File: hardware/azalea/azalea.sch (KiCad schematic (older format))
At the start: 71 parts, among them J1 USB-MICRO-B-SHIELDED, J2 USB-MICRO-B-SHIELDED, U1 LPC43XXFBD144, X1 XTAL4PIN

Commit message: azalea: neighbor interface
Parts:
- added FB? (x2): FILTER, symbol FILTER
- added P?: SPIFI_CS, symbol CONN_01X01
- added P?: LED1, symbol CONN_01X01
- added P?: LED2, symbol CONN_01X01
- added P?: LED3, symbol CONN_01X01
- added P?: LED4, symbol CONN_01X01
- added P?: USB1_VBUS, symbol CONN_01X01
- added P?: USB1_SENSE, symbol CONN_01X01
- added P?: USB1_EN, symbol CONN_01X01
- added P?: USB1_FAULT, symbol CONN_01X01
- added P?: USB1_ID, symbol CONN_01X01
- added P?: USB0_ID, symbol CONN_01X01
- added P?: P2_9, symbol CONN_01X01
- U1: value LPC43XXFBD144 -> LPC4330FBD144
- gave numbers to parts that had none: 2
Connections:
- net !CTS is gone; now on net P1_11: U1.55 (P1_11)
- net !DCD is gone; now on net P1_12: U1.56 (P1_12)
- net !DSR is gone; now on net P5_0: U1.37 (P5_0)
- net !DTR is gone; now on net P1_8: U1.51 (P1_8)
- net !RTS is gone; now on net P1_9: U1.52 (P1_9)
- net ISP is gone; now on net P2_7: R?.2, U1.96 (P2_7)
- net RXD is gone; now on net P1_14: U1.61 (P1_14)
- net SPIFI_MISO is gone; now on net P3_6: U1.122 (P3_6), U?.2 (DO)
- net SPIFI_MOSI is gone; now on net P3_7: U1.123 (P3_7), U?.5 (DI)
- net SPIFI_SCK is gone; now on net P3_3: U1.118 (P3_3), U?.6 (CLK)
- net SPIFI_SIO2 is gone; now on net P3_5: U1.121 (P3_5), U?.3 (WP)
- net SPIFI_SIO3 is gone; now on net P3_4: U1.119 (P3_4), U?.7 (HOLD)
- net TXD is gone; now on net P1_13: U1.60 (P1_13)
- net GND: now also P2.1 (P1), FB?.1, FB?.2; no longer P2.9 (P9)
- net I2C0_SCL: now also P2.40 (P40)
- net I2C0_SDA: now also P2.39 (P39)
- net LED1: now also P?.1 (P1)
- net LED2: now also P?.1 (P1)
- net LED3: now also P?.1 (P1)
- net LED4: now also P?.1 (P1)
- net P1_1: now also P1.9 (P9)
- net P1_2: now also P1.12 (P12)
- net P2_8: now also P2.27 (P27)
- net P2_9: now also P?.1 (P1)
- net SPIFI_CS: now also P?.1 (P1)
- net USB1_FAULT: now also P?.1 (P1)
- net VBUS: now also P2.2 (P2); no longer P1.3 (P3)
- net VCC: no longer P2.2 (P2), P2.4 (P4)
- net WAKEUP0: now also P2.13 (P13)
- net at J1.0 (SHIELD): now also FB?.2
- net USB0_ID: now reaches J1.4 (ID), U1.22 (USB0_ID)
- net USB0_ID: now also P?.1 (P1)
- net P4_0: now reaches U1.1 (P4_0)
- net P4_0: now also P2.11 (P11)
- net P4_5: now reaches U1.10 (P4_5)
- net P4_5: now also P2.6 (P6)
- net USB1_SENSE: now reaches R?.2, R?.2, U1.101 (P6_11)
- net USB1_SENSE: now also P?.1 (P1)
- net USB1_EN: now reaches R?.2, U1.103 (P6_12), U?.3 (EN)
- net USB1_EN: now also P?.1 (P1)
- net P4_6: now reaches U1.11 (P4_6)
- net P4_6: now also P2.5 (P5)
- net P7_0: now reaches U1.110 (P7_0)
- net P7_0: now also P2.25 (P25)
- net P3_0: now reaches U1.112 (P3_0)
- net P3_0: now also P2.24 (P24)
- net P7_1: now reaches U1.113 (P7_1)
- net P7_1: now also P2.23 (P23)
- net P3_1: now reaches U1.114 (P3_1)
- net P3_1: now also P2.22 (P22)
- net P7_2: now reaches U1.115 (P7_2)
- net P7_2: now also P2.21 (P21)
- net P3_2: now reaches U1.116 (P3_2)
- net P3_2: now also P2.20 (P20)
- net PF_4: now reaches U1.120 (PF_4)
- net PF_4: now also P2.19 (P19)
- net P4_7: now reaches U1.14 (P4_7)
- net P4_7: now also P2.4 (P4)
- net P7_7: now reaches U1.140 (P7_7)
- net P7_7: now also P2.12 (P12)
- net P4_8: now reaches U1.15 (P4_8)
- net P4_8: now also P2.3 (P3)
- net P0_0: now reaches U1.32 (P0_0)
- net P0_0: now also P1.4 (P4)
- net P4_9: now reaches U1.33 (P4_9)
- net P4_9: now also P1.3 (P3)
- net P0_1: now reaches U1.34 (P0_1)
- net P0_1: now also P1.6 (P6)
- net P4_10: now reaches U1.35 (P4_10)
- net P4_10: now also P1.5 (P5)
- net P1_0: now reaches U1.38 (P1_0)
- net P1_0: now also P1.7 (P7)
- net P5_1: now reaches U1.39 (P5_1)
- net P5_1: now also P1.10 (P10)
- net CLK0: now reaches U1.45 (CLK0)
- net CLK0: now also P1.11 (P11)
- net P5_2: now reaches U1.46 (P5_2)
- net P5_2: now also P1.14 (P14)
- net P1_5: now reaches U1.48 (P1_5)
- net P1_5: now also P1.13 (P13)
- net P1_6: now reaches U1.49 (P1_6)
- net P1_6: now also P1.16 (P16)
- net P1_7: now reaches U1.50 (P1_7)
- net P1_7: now also P1.15 (P15)
- net P1_10: now reaches U1.53 (P1_10)
- net P1_10: now also P1.20 (P20)
- net P5_3: now reaches U1.54 (P5_3)
- net P5_3: now also P1.19 (P19)
- net P5_4: now reaches U1.57 (P5_4)
- net P5_4: now also P1.24 (P24)
- net P5_5: now reaches U1.58 (P5_5)
- net P5_5: now also P1.23 (P23)
- net ADC0_0: now reaches U1.6 (ADC0_0/ADC1_0/DAC)
- net ADC0_0: now also P2.10 (P10)
- net P1_15: now reaches U1.62 (P1_15)
- net P1_15: now also P1.28 (P28)
- net P5_6: now reaches U1.63 (P5_6)
- net P5_6: now also P1.27 (P27)
- net P1_16: now reaches U1.64 (P1_16)
- net P1_16: now also P1.30 (P30)
- net P5_7: now reaches U1.65 (P5_7)
- net P5_7: now also P1.29 (P29)
- net P1_17: now reaches U1.66 (P1_17)
- net P1_17: now also P1.32 (P32)
- net P1_18: now reaches U1.67 (P1_18)
- net P1_18: now also P1.31 (P31)
- net P9_5: now reaches U1.69 (P9_5)
- net P9_5: now also P1.33 (P33)
- net P4_3: now reaches U1.7 (P4_3)
- net P4_3: now also P2.9 (P9)
- net P9_6: now reaches U1.72 (P9_6)
- net P9_6: now also P1.34 (P34)
- net P6_0: now reaches U1.73 (P6_0)
- net P6_0: now also P1.36 (P36)
- net P2_0: now reaches U1.75 (P2_0)
- net P2_0: now also P1.35 (P35)
- net P6_3: now reaches U1.79 (P6_3)
- net P6_3: now also P2.38 (P38)
- net P4_2: now reaches U1.8 (P4_2)
- net P4_2: now also P2.8 (P8)
- net P2_1: now reaches U1.81 (P2_1)
- net P2_1: now also P2.37 (P37)
- net P6_6: now reaches U1.83 (P6_6)
- net P6_6: now also P2.36 (P36)
- net P2_2: now reaches U1.84 (P2_2)
- net P2_2: now also P2.35 (P35)
- net P6_7: now reaches U1.85 (P6_7)
- net P6_7: now also P2.34 (P34)
- net P6_8: now reaches U1.86 (P6_8)
- net P6_8: now also P2.33 (P33)
- net P2_3: now reaches U1.87 (P2_3)
- net P2_3: now also P2.32 (P32)
- net P2_4: now reaches U1.88 (P2_4)
- net P2_4: now also P2.31 (P31)
- net P4_4: now reaches U1.9 (P4_4)
- net P4_4: now also P2.7 (P7)
- net P2_5: now reaches U1.91 (P2_5)
- net P2_5: now also P2.30 (P30)
- net P2_6: now reaches U1.95 (P2_6)
- net P2_6: now also P2.29 (P29)
- net CLK2: now reaches U1.99 (CLK2)
- net CLK2: now also P2.26 (P26)
- net at J2.0 (SHIELD): now also FB?.1
- net USB1_VBUS: now reaches C?.1, J2.1 (VBUS), R?.1, U?.6 (VOUT)
- net USB1_VBUS: now also P?.1 (P1)
- net USB1_ID: now reaches J2.4 (ID)
- net USB1_ID: now also P?.1 (P1)
- net P3_7: now reaches P2.14 (P14)
- net P3_6: now reaches P2.15 (P15)
- net P3_5: now reaches P2.16 (P16)
- net P3_4: now reaches P2.17 (P17)
- net P3_3: now reaches P2.18 (P18)
- net P2_7: now reaches P2.28 (P28)
- net P1_9: now reaches P1.17 (P17)
- net P1_8: now reaches P1.18 (P18)
- net P1_12: now reaches P1.21 (P21)
- net P1_11: now reaches P1.22 (P22)
- net P1_14: now reaches P1.25 (P25)
- net P1_13: now reaches P1.26 (P26)
- net P1_19: now reaches P1.37 (P37)
- net P1_19: now also U1.68 (P1_19)
- net P1_20: now reaches P1.38 (P38)
- net P1_20: now also U1.70 (P1_20)
- net P1_3: now reaches P1.39 (P39)
- net P1_3: now also U1.44 (P1_3)
- net P1_4: now reaches P1.40 (P40)
- net P1_4: now also U1.47 (P1_4)
- net P5_0: now reaches P1.8 (P8)
- removed net MISO: P2.1 (P1), U1.44 (P1_3)
- removed net MOSI: P2.3 (P3), U1.47 (P1_4)
- removed net SCK: P2.7 (P7), U1.68 (P1_19)
- removed net SSEL: P2.5 (P5), U1.70 (P1_20)
- no-connect marks 19 -> 18
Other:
- note added: "BOOT"
- note added: "DFU"
- note added: "ISP"
- note added: "MISO"
- note added: "MOSI"
- note added: "SCK"
- note added: "SSEL"
- note removed: "TODO\n\nneighbor interface"
- moved on the sheet: C?, R?, U?

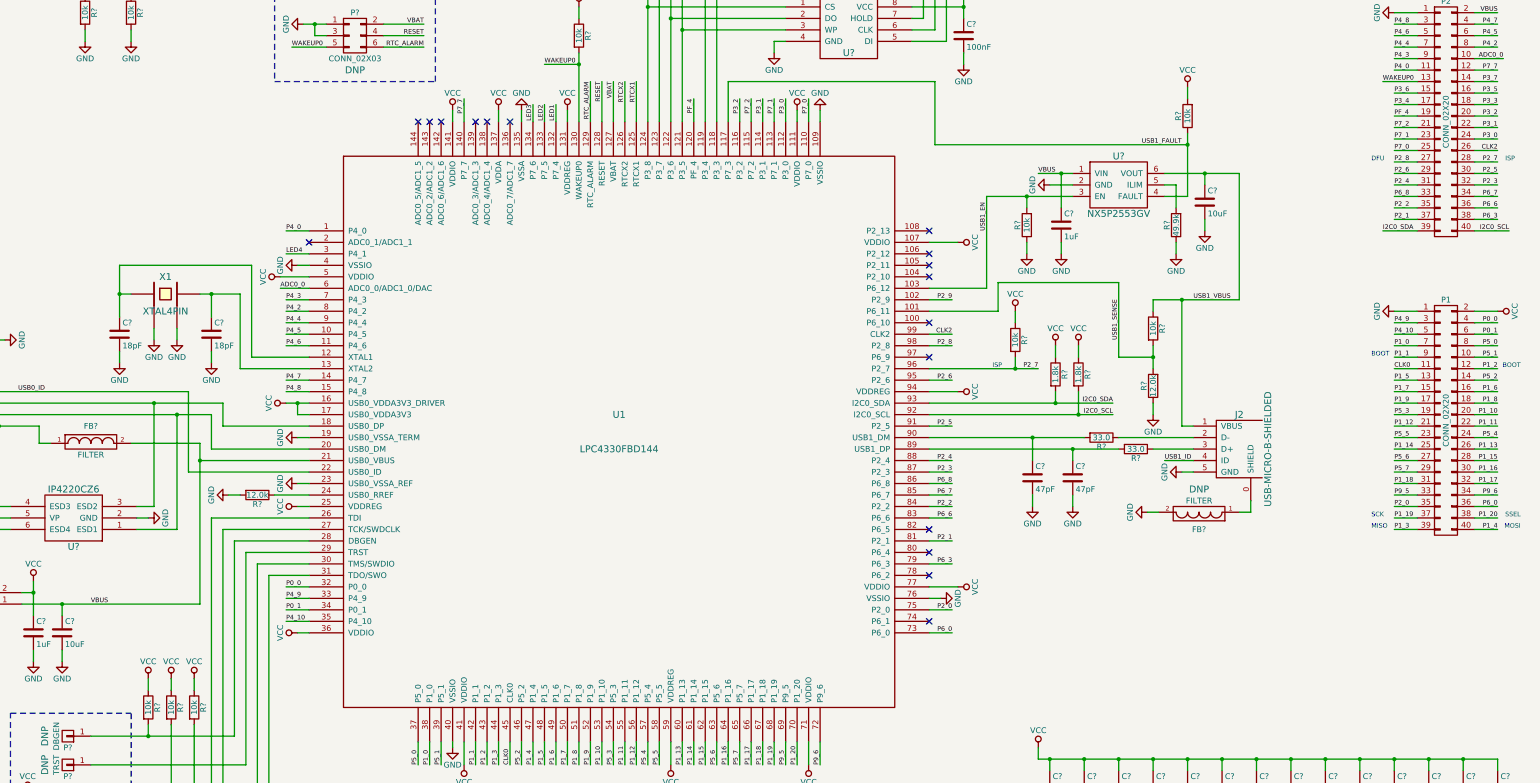
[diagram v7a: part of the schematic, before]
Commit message: azalea: bonus row of pins that might get cut
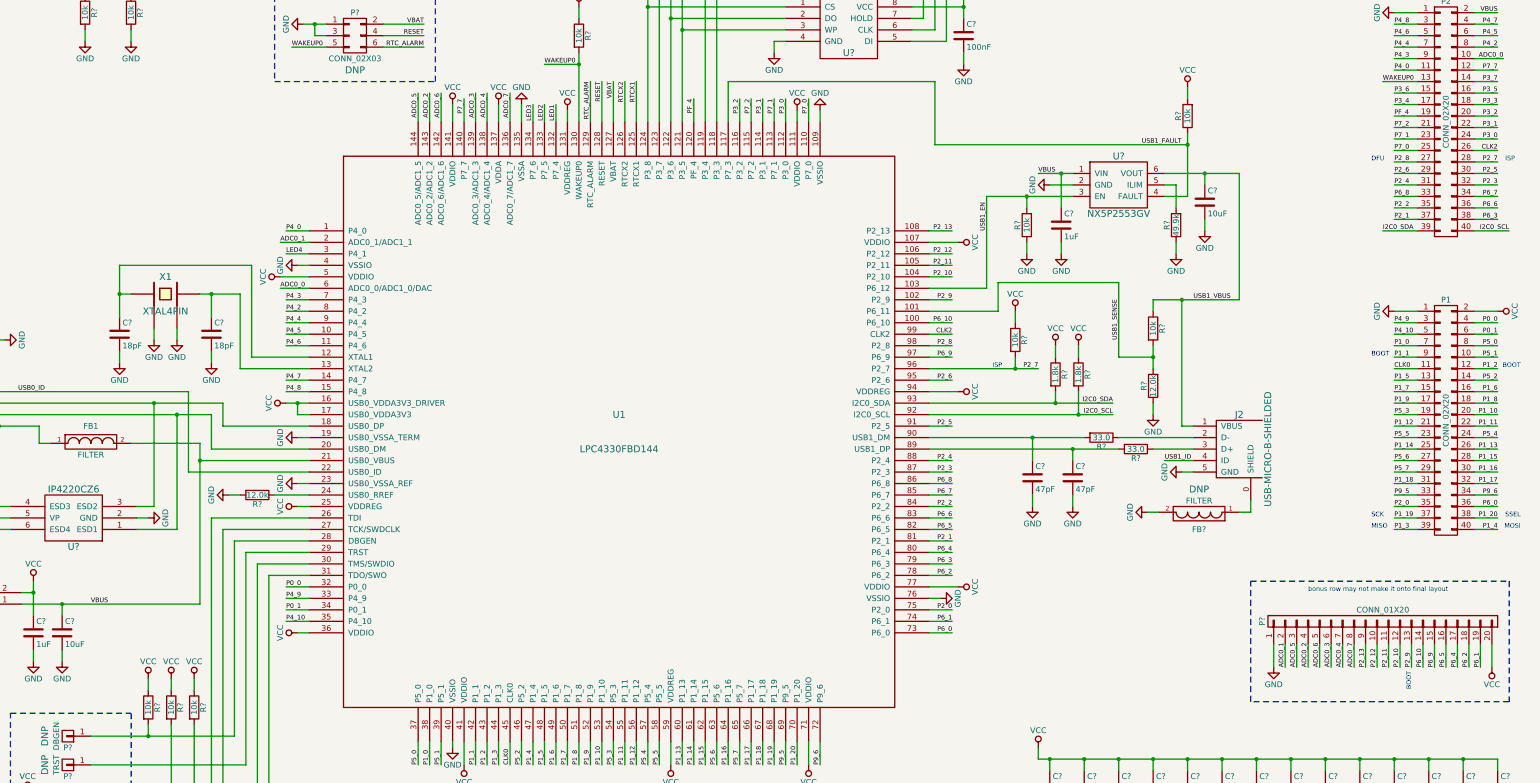
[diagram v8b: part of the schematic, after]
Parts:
- added P?: CONN_01X20, symbol CONN_01X20
- gave numbers to parts that had none: 1
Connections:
- net GND: now also P?.1 (P1)
- net P2_9: now also P?.13 (P13)
- net VCC: now also P?.20 (P20)
- net P6_10: now reaches U1.100 (P6_10)
- net P6_10: now also P?.14 (P14)
- net P2_10: now reaches U1.104 (P2_10)
- net P2_10: now also P?.12 (P12)
- net P2_11: now reaches U1.105 (P2_11)
- net P2_11: now also P?.11 (P11)
- net P2_12: now reaches U1.106 (P2_12)
- net P2_12: now also P?.10 (P10)
- net P2_13: now reaches U1.108 (P2_13)
- net P2_13: now also P?.9 (P9)
- net ADC0_7: now reaches U1.136 (ADC0_7/ADC1_7)
- net ADC0_7: now also P?.8 (P8)
- net ADC0_4: now reaches U1.138 (ADC0_4/ADC1_4)
- net ADC0_4: now also P?.7 (P7)
- net ADC0_3: now reaches U1.139 (ADC0_3/ADC1_3)
- net ADC0_3: now also P?.6 (P6)
- net ADC0_6: now reaches U1.142 (ADC0_6/ADC1_6)
- net ADC0_6: now also P?.5 (P5)
- net ADC0_2: now reaches U1.143 (ADC0_2/ADC1_2)
- net ADC0_2: now also P?.4 (P4)
- net ADC0_5: now reaches U1.144 (ADC0_5/ADC1_5)
- net ADC0_5: now also P?.3 (P3)
- net ADC0_1: now reaches U1.2 (ADC0_1/ADC1_1)
- net ADC0_1: now also P?.2 (P2)
- net P6_1: now reaches U1.74 (P6_1)
- net P6_1: now also P?.19 (P19)
- net P6_2: now reaches U1.78 (P6_2)
- net P6_2: now also P?.18 (P18)
- net P6_4: now reaches U1.80 (P6_4)
- net P6_4: now also P?.17 (P17)
- net P6_5: now reaches U1.82 (P6_5)
- net P6_5: now also P?.16 (P16)
- net P6_9: now reaches U1.97 (P6_9)
- net P6_9: now also P?.15 (P15)
- no-connect marks 18 -> 1
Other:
- note added: "bonus row may not make it onto final layout"
